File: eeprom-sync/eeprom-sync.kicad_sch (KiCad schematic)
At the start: 8 parts

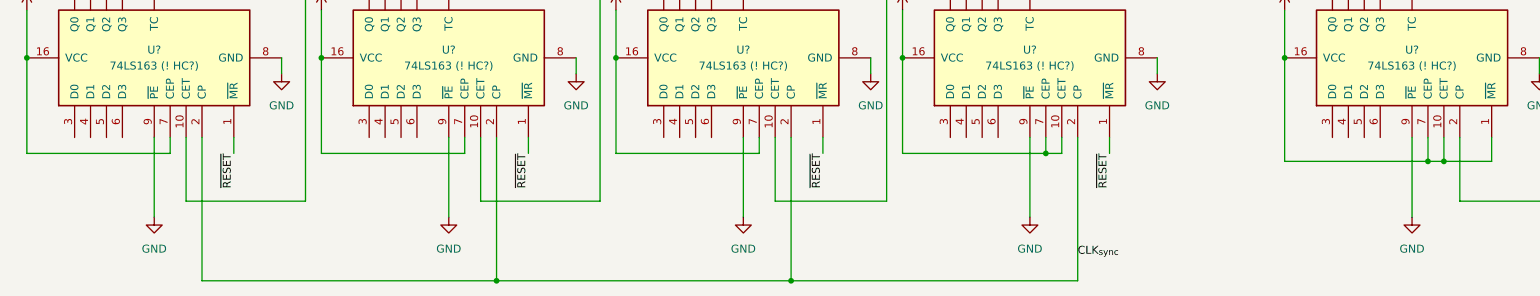
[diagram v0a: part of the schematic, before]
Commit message: fix(sync): /LOAD is active low, don't ground it
Previously, all the /LOAD pins (/PE on the diagram) were wired to ground,
but the intention was to disable the "preloading" feature entirely, which
this change accomplishes by tying them high instead.
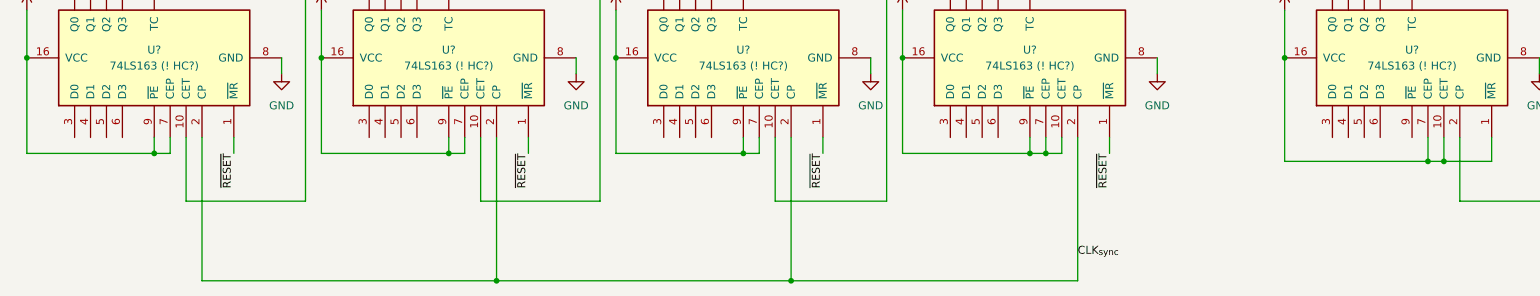
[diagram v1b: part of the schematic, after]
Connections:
- net GND: no longer U?.9 (~{PE}), U?.9 (~{PE}), U?.9 (~{PE}), U?.9 (~{PE}), U?.9 (~{PE})
- net VCC: now also U?.9 (~{PE}), U?.9 (~{PE}), U?.9 (~{PE}), U?.9 (~{PE})
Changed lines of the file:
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@@
   (junction (at 137.16 154.94) (diameter 0) (color 0 0 0 0)
   )
+  (junction (at 35.56 134.62) (diameter 0) (color 0 0 0 0)
+  )
   (junction (at 15.24 119.38) (diameter 0) (color 0 0 0 0)
   )
@@
   (junction (at 106.68 20.32) (diameter 0) (color 0 0 0 0)
   )
+  (junction (at 175.26 134.62) (diameter 0) (color 0 0 0 0)
+  )
   (junction (at 62.23 119.38) (diameter 0) (color 0 0 0 0)
   )
+  (junction (at 129.54 134.62) (diameter 0) (color 0 0 0 0)
+  )
   (junction (at 215.9 119.38) (diameter 0) (color 0 0 0 0)
   )
@@
   (junction (at 177.8 134.62) (diameter 0) (color 0 0 0 0)
   )
+  (junction (at 82.55 134.62) (diameter 0) (color 0 0 0 0)
+  )
   (junction (at 148.59 72.39) (diameter 0) (color 0 0 0 0)
   )
@@
     (stroke (width 0) (type default) (color 0 0 0 0))
   )
-  (wire (pts (xy 15.24 134.62) (xy 38.1 134.62))
+  (wire (pts (xy 15.24 134.62) (xy 35.56 134.62))
     (stroke (width 0) (type default) (color 0 0 0 0))
   )
@@
     (stroke (width 0) (type default) (color 0 0 0 0))
   )
-  (wire (pts (xy 175.26 132.08) (xy 175.26 144.78))
-    (stroke (width 0) (type default) (color 0 0 0 0))
-  )
   (bus (pts (xy 162.56 102.87) (xy 165.1 102.87))
     (stroke (width 0) (type default) (color 0 0 0 0))
@@
     (stroke (width 0) (type default) (color 0 0 0 0))
   )
+  (wire (pts (xy 175.26 132.08) (xy 175.26 134.62))
+    (stroke (width 0) (type default) (color 0 0 0 0))
+  )
   (wire (pts (xy 116.84 34.29) (xy 135.89 44.45))
     (stroke (width 0) (type default) (color 0 0 0 0))
@@
     (stroke (width 0) (type default) (color 0 0 0 0))
   )
-  (wire (pts (xy 154.94 134.62) (xy 177.8 134.62))
+  (wire (pts (xy 154.94 134.62) (xy 175.26 134.62))
     (stroke (width 0) (type default) (color 0 0 0 0))
   )
@@
     (stroke (width 0) (type default) (color 0 0 0 0))
   )
+  (wire (pts (xy 129.54 132.08) (xy 129.54 134.62))
+    (stroke (width 0) (type default) (color 0 0 0 0))
+  )
   (wire (pts (xy 15.24 111.76) (xy 15.24 119.38))
     (stroke (width 0) (type default) (color 0 0 0 0))
@@
     (stroke (width 0) (type default) (color 0 0 0 0))
   )
-  (wire (pts (xy 129.54 132.08) (xy 129.54 144.78))
-    (stroke (width 0) (type default) (color 0 0 0 0))
-  )
   (wire (pts (xy 92.71 74.93) (xy 92.71 81.28))
     (stroke (width 0) (type default) (color 0 0 0 0))
@@
     (stroke (width 0) (type default) (color 0 0 0 0))
   )
-  (wire (pts (xy 82.55 132.08) (xy 82.55 144.78))
-    (stroke (width 0) (type default) (color 0 0 0 0))
-  )
   (wire (pts (xy 116.84 39.37) (xy 135.89 49.53))
     (stroke (width 0) (type default) (color 0 0 0 0))
@@
     (stroke (width 0) (type default) (color 0 0 0 0))
   )
+  (wire (pts (xy 129.54 134.62) (xy 132.08 134.62))
+    (stroke (width 0) (type default) (color 0 0 0 0))
+  )
   (wire (pts (xy 95.25 31.75) (xy 96.52 31.75))
     (stroke (width 0) (type default) (color 0 0 0 0))
   )
+  (wire (pts (xy 175.26 134.62) (xy 177.8 134.62))
+    (stroke (width 0) (type default) (color 0 0 0 0))
+  )
   (wire (pts (xy 215.9 119.38) (xy 215.9 135.89))
     (stroke (width 0) (type default) (color 0 0 0 0))
   )
+  (wire (pts (xy 82.55 134.62) (xy 85.09 134.62))
+    (stroke (width 0) (type default) (color 0 0 0 0))
+  )
   (wire (pts (xy 74.93 105.41) (xy 74.93 106.68))
     (stroke (width 0) (type default) (color 0 0 0 0))
@@
     (stroke (width 0) (type default) (color 0 0 0 0))
   )
+  (wire (pts (xy 82.55 132.08) (xy 82.55 134.62))
+    (stroke (width 0) (type default) (color 0 0 0 0))
+  )
   (wire (pts (xy 83.82 20.32) (xy 106.68 20.32))
     (stroke (width 0) (type default) (color 0 0 0 0))
@@
     (stroke (width 0) (type default) (color 0 0 0 0))
   )
+  (wire (pts (xy 35.56 132.08) (xy 35.56 134.62))
+    (stroke (width 0) (type default) (color 0 0 0 0))
+  )
   (bus (pts (xy 92.71 57.15) (xy 92.71 54.61))
     (stroke (width 0) (type default) (color 0 0 0 0))
@@
     (stroke (width 0) (type default) (color 0 0 0 0))
   )
-  (wire (pts (xy 35.56 132.08) (xy 35.56 144.78))
-    (stroke (width 0) (type default) (color 0 0 0 0))
-  )
   (wire (pts (xy 96.52 72.39) (xy 92.71 72.39))
     (stroke (width 0) (type default) (color 0 0 0 0))
@@
     (stroke (width 0) (type default) (color 0 0 0 0))
   )
-  (wire (pts (xy 236.22 132.08) (xy 236.22 144.78))
-    (stroke (width 0) (type default) (color 0 0 0 0))
-  )
   (wire (pts (xy 116.84 36.83) (xy 135.89 46.99))
     (stroke (width 0) (type default) (color 0 0 0 0))
@@
     (stroke (width 0) (type default) (color 0 0 0 0))
   )
-  (wire (pts (xy 62.23 134.62) (xy 85.09 134.62))
+  (wire (pts (xy 62.23 134.62) (xy 82.55 134.62))
     (stroke (width 0) (type default) (color 0 0 0 0))
   )
@@
     (stroke (width 0) (type default) (color 0 0 0 0))
   )
+  (wire (pts (xy 35.56 134.62) (xy 38.1 134.62))
+    (stroke (width 0) (type default) (color 0 0 0 0))
+  )
   (bus (pts (xy 92.71 31.75) (xy 92.71 29.21))
     (stroke (width 0) (type default) (color 0 0 0 0))
@@
     (stroke (width 0) (type default) (color 0 0 0 0))
   )
-  (wire (pts (xy 109.22 134.62) (xy 132.08 134.62))
+  (wire (pts (xy 109.22 134.62) (xy 129.54 134.62))
     (stroke (width 0) (type default) (color 0 0 0 0))
   )
@@
     (pin "1")
   )
-  (symbol (lib_id "power:GND") (at 35.56 144.78 0) (unit 1)
-    (in_bom yes) (on_board yes) (fields_autoplaced)
-    (property "Reference" "#PWR?" (id 0) (at 35.56 151.13 0)
-      (effects (font (size 1.27 1.27)) hide)
-    )
-    (property "Value" "GND" (id 1) (at 35.56 149.86 0))
-    (property "Footprint" "" (id 2) (at 35.56 144.78 0)
-      (effects (font (size 1.27 1.27)) hide)
-    )
-    (property "Datasheet" "" (id 3) (at 35.56 144.78 0)
-      (effects (font (size 1.27 1.27)) hide)
-    )
-    (pin "1")
-  )
   (symbol (lib_id "power:GND") (at 55.88 121.92 0) (unit 1)
     (in_bom yes) (on_board yes) (fields_autoplaced)
@@
     (pin "1")
   )
-  (symbol (lib_id "power:GND") (at 129.54 144.78 0) (unit 1)
-    (in_bom yes) (on_board yes) (fields_autoplaced)
-    (property "Reference" "#PWR?" (id 0) (at 129.54 151.13 0)
-      (effects (font (size 1.27 1.27)) hide)
-    )
-    (property "Value" "GND" (id 1) (at 129.54 149.86 0))
-    (property "Footprint" "" (id 2) (at 129.54 144.78 0)
-      (effects (font (size 1.27 1.27)) hide)
-    )
-    (property "Datasheet" "" (id 3) (at 129.54 144.78 0)
-      (effects (font (size 1.27 1.27)) hide)
-    )
-    (pin "1")
-  )
   (symbol (lib_id "power:VCC") (at 154.94 111.76 0) (unit 1)
     (in_bom yes) (on_board yes) (fields_autoplaced)
@@
     )
     (property "Datasheet" "" (id 3) (at 106.68 20.32 0)
-      (effects (font (size 1.27 1.27)) hide)
-    )
-    (pin "1")
-  )
-  (symbol (lib_id "power:GND") (at 236.22 144.78 0) (unit 1)
-    (in_bom yes) (on_board yes) (fields_autoplaced)
-    (property "Reference" "#PWR?" (id 0) (at 236.22 151.13 0)
-      (effects (font (size 1.27 1.27)) hide)
-    )
-    (property "Value" "GND" (id 1) (at 236.22 149.86 0))
-    (property "Footprint" "" (id 2) (at 236.22 144.78 0)
-      (effects (font (size 1.27 1.27)) hide)
-    )
-    (property "Datasheet" "" (id 3) (at 236.22 144.78 0)
       (effects (font (size 1.27 1.27)) hide)
     )
@@
     (pin "1")
   )
-  (symbol (lib_id "power:GND") (at 175.26 144.78 0) (unit 1)
-    (in_bom yes) (on_board yes) (fields_autoplaced)
-    (property "Reference" "#PWR?" (id 0) (at 175.26 151.13 0)
-      (effects (font (size 1.27 1.27)) hide)
-    )
-    (property "Value" "GND" (id 1) (at 175.26 149.86 0))
-    (property "Footprint" "" (id 2) (at 175.26 144.78 0)
-      (effects (font (size 1.27 1.27)) hide)
-    )
-    (property "Datasheet" "" (id 3) (at 175.26 144.78 0)
-      (effects (font (size 1.27 1.27)) hide)
-    )
-    (pin "1")
-  )
   (symbol (lib_id "74xx:74HCT574") (at 148.59 52.07 0) (unit 1)
     (in_bom yes) (on_board yes) (fields_autoplaced)
@@
     (pin "9")
   )
-  (symbol (lib_id "power:GND") (at 82.55 144.78 0) (unit 1)
-    (in_bom yes) (on_board yes) (fields_autoplaced)
-    (property "Reference" "#PWR?" (id 0) (at 82.55 151.13 0)
-      (effects (font (size 1.27 1.27)) hide)
-    )
-    (property "Value" "GND" (id 1) (at 82.55 149.86 0))
-    (property "Footprint" "" (id 2) (at 82.55 144.78 0)
-      (effects (font (size 1.27 1.27)) hide)
-    )
-    (property "Datasheet" "" (id 3) (at 82.55 144.78 0)
-      (effects (font (size 1.27 1.27)) hide)
-    )
-    (pin "1")
-  )
   (sheet_instances
     (path "/" (page "1"))
@@
       (reference "#PWR?") (unit 1) (value "GND") (footprint "")
     )
-    (path "/93c54f3c-9322-4464-a82a-12b22182647b"
-      (reference "#PWR?") (unit 1) (value "GND") (footprint "")
-    )
     (path "/9466fadc-b23b-4a39-9815-66e768fe492b"
       (reference "#PWR?") (unit 1) (value "GND") (footprint "")
     )
-    (path "/95db3b83-1c2e-4948-99a0-7e3149a40fbc"
-      (reference "#PWR?") (unit 1) (value "GND") (footprint "")
-    )
     (path "/9ee2e8b1-1894-47b8-8f54-acf5e958ed4b"
       (reference "#PWR?") (unit 1) (value "VCC") (footprint "")
@@
       (reference "#PWR?") (unit 1) (value "VCC") (footprint "")
     )
-    (path "/a1cbfc35-fccf-4d80-8b79-6f0f7432413e"
-      (reference "#PWR?") (unit 1) (value "GND") (footprint "")
-    )
     (path "/ca4c22d6-c73c-47aa-9896-4a7fbd289d4e"
       (reference "#PWR?") (unit 1) (value "GND") (footprint "")
@@
       (reference "#PWR?") (unit 1) (value "VCC") (footprint "")
     )
-    (path "/d47f5066-515b-415c-8a8e-f5a1b610895c"
-      (reference "#PWR?") (unit 1) (value "GND") (footprint "")
-    )
-    (path "/f5c014e2-b931-413b-80c4-f984be1061d9"
-      (reference "#PWR?") (unit 1) (value "GND") (footprint "")
-    )
     (path "/344a357d-dce8-44dd-b35e-a92077988cd9"

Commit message: wip(eeprom): move ~{RESET}, update bits->pins
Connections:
- net HSync: now also U?.18 (Q1); no longer U?.19 (Q0)
- net VSync: now also U?.16 (Q3); no longer U?.18 (Q1)
- net Vis: now also U?.15 (Q4); no longer U?.17 (Q2)
- net ~{RESET}: now also U?.19 (D7), U?.9 (D7); no longer U?.12 (Q7)
- new net HVis: U?.19 (Q0)
- new net VertVis: U?.17 (Q2)
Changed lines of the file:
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@@
   (junction (at 238.76 135.89) (diameter 0) (color 0 0 0 0)
   )
+  (junction (at 116.84 46.99) (diameter 0) (color 0 0 0 0)
+  )
   (junction (at 241.3 135.89) (diameter 0) (color 0 0 0 0)
   )
@@
     (stroke (width 0) (type default) (color 0 0 0 0))
   )
+  (wire (pts (xy 173.99 49.53) (xy 173.99 50.8))
+    (stroke (width 0) (type default) (color 0 0 0 0))
+  )
   (wire (pts (xy 116.84 105.41) (xy 116.84 106.68))
     (stroke (width 0) (type default) (color 0 0 0 0))
@@
     (stroke (width 0) (type default) (color 0 0 0 0))
   )
-  (wire (pts (xy 167.64 43.18) (xy 176.53 43.18))
-    (stroke (width 0) (type default) (color 0 0 0 0))
-  )
   (wire (pts (xy 215.9 111.76) (xy 215.9 119.38))
     (stroke (width 0) (type default) (color 0 0 0 0))
@@
     (stroke (width 0) (type default) (color 0 0 0 0))
   )
+  (wire (pts (xy 172.72 54.61) (xy 179.07 54.61))
+    (stroke (width 0) (type default) (color 0 0 0 0))
+  )
   (bus (pts (xy 162.56 102.87) (xy 165.1 102.87))
     (stroke (width 0) (type default) (color 0 0 0 0))
@@
     (stroke (width 0) (type default) (color 0 0 0 0))
   )
+  (wire (pts (xy 173.99 45.72) (xy 179.07 45.72))
+    (stroke (width 0) (type default) (color 0 0 0 0))
+  )
   (bus (pts (xy 92.71 49.53) (xy 92.71 46.99))
     (stroke (width 0) (type default) (color 0 0 0 0))
@@
     (stroke (width 0) (type default) (color 0 0 0 0))
   )
+  (wire (pts (xy 161.29 52.07) (xy 172.72 52.07))
+    (stroke (width 0) (type default) (color 0 0 0 0))
+  )
   (wire (pts (xy 43.18 154.94) (xy 43.18 132.08))
     (stroke (width 0) (type default) (color 0 0 0 0))
   )
-  (wire (pts (xy 165.1 46.99) (xy 176.53 46.99))
-    (stroke (width 0) (type default) (color 0 0 0 0))
-  )
   (wire (pts (xy 90.17 132.08) (xy 90.17 154.94))
     (stroke (width 0) (type default) (color 0 0 0 0))
@@
     (stroke (width 0) (type default) (color 0 0 0 0))
   )
+  (wire (pts (xy 170.18 58.42) (xy 179.07 58.42))
+    (stroke (width 0) (type default) (color 0 0 0 0))
+  )
   (wire (pts (xy 195.58 119.38) (xy 195.58 121.92))
     (stroke (width 0) (type default) (color 0 0 0 0))
@@
     (stroke (width 0) (type default) (color 0 0 0 0))
   )
-  (wire (pts (xy 161.29 39.37) (xy 176.53 39.37))
-    (stroke (width 0) (type default) (color 0 0 0 0))
-  )
   (wire (pts (xy 92.71 81.28) (xy 106.68 81.28))
     (stroke (width 0) (type default) (color 0 0 0 0))
@@
     (stroke (width 0) (type default) (color 0 0 0 0))
   )
-  (wire (pts (xy 165.1 44.45) (xy 165.1 46.99))
-    (stroke (width 0) (type default) (color 0 0 0 0))
-  )
   (wire (pts (xy 149.86 119.38) (xy 149.86 121.92))
     (stroke (width 0) (type default) (color 0 0 0 0))
@@
     (stroke (width 0) (type default) (color 0 0 0 0))
   )
+  (wire (pts (xy 167.64 39.37) (xy 167.64 34.29))
+    (stroke (width 0) (type default) (color 0 0 0 0))
+  )
+  (wire (pts (xy 170.18 41.91) (xy 170.18 38.1))
+    (stroke (width 0) (type default) (color 0 0 0 0))
+  )
   (wire (pts (xy 77.47 105.41) (xy 77.47 106.68))
     (stroke (width 0) (type default) (color 0 0 0 0))
@@
     (stroke (width 0) (type default) (color 0 0 0 0))
   )
+  (wire (pts (xy 172.72 41.91) (xy 179.07 41.91))
+    (stroke (width 0) (type default) (color 0 0 0 0))
+  )
   (wire (pts (xy 106.68 80.01) (xy 106.68 81.28))
     (stroke (width 0) (type default) (color 0 0 0 0))
   )
+  (wire (pts (xy 173.99 50.8) (xy 179.07 50.8))
+    (stroke (width 0) (type default) (color 0 0 0 0))
+  )
+  (wire (pts (xy 161.29 54.61) (xy 170.18 54.61))
+    (stroke (width 0) (type default) (color 0 0 0 0))
+  )
   (wire (pts (xy 116.84 39.37) (xy 135.89 49.53))
     (stroke (width 0) (type default) (color 0 0 0 0))
@@
     (stroke (width 0) (type default) (color 0 0 0 0))
   )
-  (wire (pts (xy 161.29 57.15) (xy 176.53 57.15))
+  (wire (pts (xy 170.18 54.61) (xy 170.18 58.42))
     (stroke (width 0) (type default) (color 0 0 0 0))
   )
@@
     (stroke (width 0) (type default) (color 0 0 0 0))
   )
-  (wire (pts (xy 161.29 41.91) (xy 167.64 41.91))
-    (stroke (width 0) (type default) (color 0 0 0 0))
-  )
   (wire (pts (xy 116.84 31.75) (xy 135.89 41.91))
     (stroke (width 0) (type default) (color 0 0 0 0))
   )
+  (wire (pts (xy 161.29 44.45) (xy 172.72 44.45))
+    (stroke (width 0) (type default) (color 0 0 0 0))
+  )
+  (wire (pts (xy 161.29 39.37) (xy 167.64 39.37))
+    (stroke (width 0) (type default) (color 0 0 0 0))
+  )
   (wire (pts (xy 175.26 93.98) (xy 152.4 93.98))
     (stroke (width 0) (type default) (color 0 0 0 0))
@@
     (stroke (width 0) (type default) (color 0 0 0 0))
   )
+  (wire (pts (xy 161.29 41.91) (xy 170.18 41.91))
+    (stroke (width 0) (type default) (color 0 0 0 0))
+  )
   (wire (pts (xy 129.54 134.62) (xy 132.08 134.62))
     (stroke (width 0) (type default) (color 0 0 0 0))
@@
     (stroke (width 0) (type default) (color 0 0 0 0))
   )
+  (wire (pts (xy 173.99 46.99) (xy 173.99 45.72))
+    (stroke (width 0) (type default) (color 0 0 0 0))
+  )
   (wire (pts (xy 82.55 132.08) (xy 82.55 134.62))
     (stroke (width 0) (type default) (color 0 0 0 0))
@@
     (stroke (width 0) (type default) (color 0 0 0 0))
   )
-  (wire (pts (xy 161.29 44.45) (xy 165.1 44.45))
-    (stroke (width 0) (type default) (color 0 0 0 0))
-  )
   (wire (pts (xy 48.26 132.08) (xy 48.26 134.62))
     (stroke (width 0) (type default) (color 0 0 0 0))
@@
     (stroke (width 0) (type default) (color 0 0 0 0))
   )
+  (wire (pts (xy 170.18 38.1) (xy 179.07 38.1))
+    (stroke (width 0) (type default) (color 0 0 0 0))
+  )
   (bus (pts (xy 72.39 102.87) (xy 74.93 102.87))
     (stroke (width 0) (type default) (color 0 0 0 0))
@@
     (stroke (width 0) (type default) (color 0 0 0 0))
   )
+  (wire (pts (xy 161.29 49.53) (xy 173.99 49.53))
+    (stroke (width 0) (type default) (color 0 0 0 0))
+  )
   (wire (pts (xy 59.69 142.24) (xy 40.64 142.24))
     (stroke (width 0) (type default) (color 0 0 0 0))
@@
     (stroke (width 0) (type default) (color 0 0 0 0))
   )
+  (wire (pts (xy 172.72 44.45) (xy 172.72 41.91))
+    (stroke (width 0) (type default) (color 0 0 0 0))
+  )
   (wire (pts (xy 170.18 105.41) (xy 170.18 106.68))
     (stroke (width 0) (type default) (color 0 0 0 0))
@@
     (stroke (width 0) (type default) (color 0 0 0 0))
   )
+  (wire (pts (xy 116.84 72.39) (xy 123.19 72.39))
+    (stroke (width 0) (type default) (color 0 0 0 0))
+  )
   (wire (pts (xy 256.54 119.38) (xy 256.54 121.92))
     (stroke (width 0) (type default) (color 0 0 0 0))
@@
     (stroke (width 0) (type default) (color 0 0 0 0))
   )
+  (wire (pts (xy 172.72 52.07) (xy 172.72 54.61))
+    (stroke (width 0) (type default) (color 0 0 0 0))
+  )
   (wire (pts (xy 106.68 93.98) (xy 106.68 142.24))
     (stroke (width 0) (type default) (color 0 0 0 0))
   )
-  (wire (pts (xy 167.64 41.91) (xy 167.64 43.18))
-    (stroke (width 0) (type default) (color 0 0 0 0))
-  )
   (wire (pts (xy 243.84 142.24) (xy 243.84 132.08))
     (stroke (width 0) (type default) (color 0 0 0 0))
   )
+  (wire (pts (xy 167.64 34.29) (xy 179.07 34.29))
+    (stroke (width 0) (type default) (color 0 0 0 0))
+  )
+  (wire (pts (xy 161.29 46.99) (xy 173.99 46.99))
+    (stroke (width 0) (type default) (color 0 0 0 0))
+  )
   (wire (pts (xy 241.3 135.89) (xy 248.92 135.89))
     (stroke (width 0) (type default) (color 0 0 0 0))
@@
   )
   (wire (pts (xy 95.25 52.07) (xy 96.52 52.07))
+    (stroke (width 0) (type default) (color 0 0 0 0))
+  )
+  (wire (pts (xy 116.84 46.99) (xy 116.84 72.39))
     (stroke (width 0) (type default) (color 0 0 0 0))
   )
@@
     (effects (font (size 1.27 1.27)) (justify right bottom))
   )
-  (label "~{RESET}" (at 176.53 57.15 0)
+  (label "~{RESET}" (at 123.19 72.39 0)
     (effects (font (size 1.27 1.27)) (justify left bottom))
   )
@@
     (effects (font (size 1.27 1.27)) (justify right bottom))
   )
-  (global_label "Vis" (shape input) (at 176.53 46.99 0) (fields_autoplaced)
+  (global_label "Vis" (shape input) (at 179.07 50.8 0) (fields_autoplaced)
     (effects (font (size 1.27 1.27)) (justify left))
-    (property "Intersheet References" "${INTERSHEET_REFS}" (id 0) (at 181.6645 46.9106 0)
+    (property "Intersheet References" "${INTERSHEET_REFS}" (id 0) (at 184.2045 50.7206 0)
       (effects (font (size 1.27 1.27)) (justify left) hide)
     )
   )
-  (global_label "VSync" (shape input) (at 176.53 43.18 0) (fields_autoplaced)
+  (global_label "VertVis" (shape input) (at 179.07 41.91 0) (fields_autoplaced)
     (effects (font (size 1.27 1.27)) (justify left))
-    (property "Intersheet References" "${INTERSHEET_REFS}" (id 0) (at 184.4464 43.1006 0)
+    (property "Intersheet References" "${INTERSHEET_REFS}" (id 0) (at 187.8936 41.8306 0)
       (effects (font (size 1.27 1.27)) (justify left) hide)
     )
   )
-  (global_label "HSync" (shape input) (at 176.53 39.37 0) (fields_autoplaced)
+  (global_label "VSync" (shape input) (at 179.07 45.72 0) (fields_autoplaced)
     (effects (font (size 1.27 1.27)) (justify left))
-    (property "Intersheet References" "${INTERSHEET_REFS}" (id 0) (at 184.6883 39.2906 0)
+    (property "Intersheet References" "${INTERSHEET_REFS}" (id 0) (at 186.9864 45.6406 0)
       (effects (font (size 1.27 1.27)) (justify left) hide)
     )
+  )
+  (global_label "HVis" (shape input) (at 179.07 34.29 0) (fields_autoplaced)
+    (effects (font (size 1.27 1.27)) (justify left))
+    (property "Intersheet References" "${INTERSHEET_REFS}" (id 0) (at 185.535 34.2106 0)
+      (effects (font (size 1.27 1.27)) (justify left) hide)
+    )
+  )
+  (global_label "HSync" (shape input) (at 179.07 38.1 0) (fields_autoplaced)
+    (effects (font (size 1.27 1.27)) (justify left))
+    (property "Intersheet References" "${INTERSHEET_REFS}" (id 0) (at 187.2283 38.0206 0)
+      (effects (font (size 1.27 1.27)) (justify left) hide)
+    )
